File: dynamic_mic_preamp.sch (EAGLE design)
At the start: 13 parts

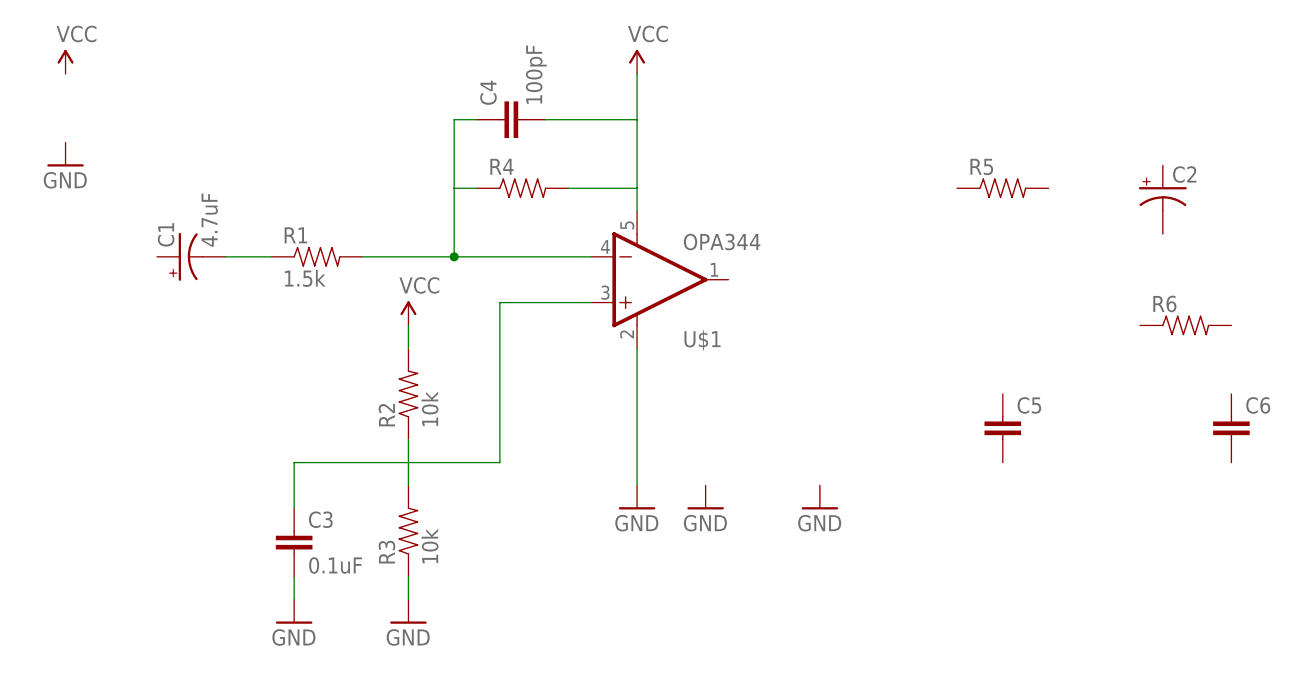
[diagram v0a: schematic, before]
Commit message: roughing out pre-amp schematic
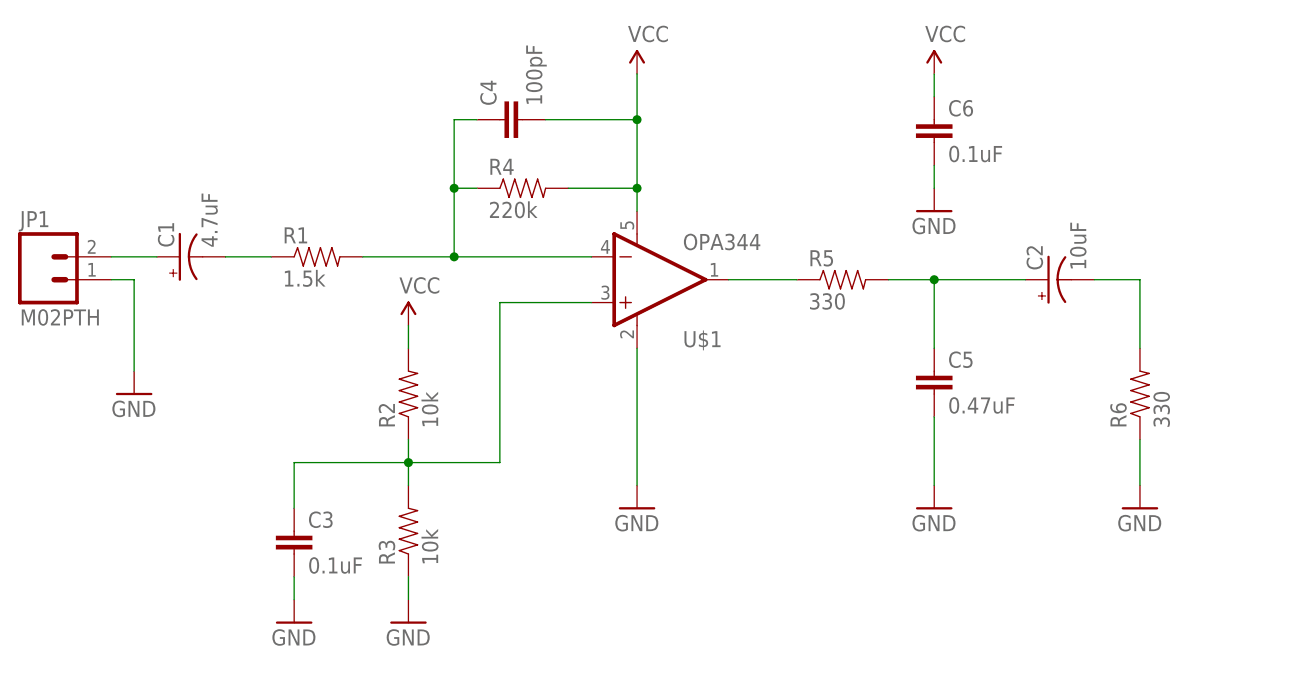
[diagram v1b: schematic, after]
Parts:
- added JP1: M02PTH, SparkFun-Connectors:M02PTH
- C2: value (none) -> 10uF
- C5: value (none) -> 0.47uF
- C6: value (none) -> 0.1uF
- R4: value (none) -> 220k
- R5, R6: value (none) -> 330
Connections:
- new net N$4: R5.1, U$1.OUT
- new net N$5: C2.+, C5.1, R5.2
- new net N$6: C2.-, R6.2
- new net N$7: C1.+, JP1.2
- net GND: now also C5.2, C6.2, JP1.1, R6.1
- net VCC: now also C6.1
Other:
- moved on the sheet: C2, C5, C6, R5, R6
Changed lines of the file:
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@@
 <parts>
 <part name="C1" library="SparkFun-Passives" deviceset="CAP_POL" device="PTH1" value="4.7uF"/>
-<part name="C2" library="SparkFun-Passives" deviceset="CAP_POL" device="PTH1"/>
+<part name="C2" library="SparkFun-Passives" deviceset="CAP_POL" device="PTH1" value="10uF"/>
 <part name="C3" library="SparkFun-Passives" deviceset="CAP" device="PTH" value="0.1uF"/>
 <part name="C4" library="SparkFun-Passives" deviceset="CAP" device="PTH" value="100pF"/>
-<part name="C5" library="SparkFun-Passives" deviceset="CAP" device="PTH"/>
-<part name="C6" library="SparkFun-Passives" deviceset="CAP" device="PTH"/>
+<part name="C5" library="SparkFun-Passives" deviceset="CAP" device="PTH" value="0.47uF"/>
 <part name="U$1" library="SparkFun-AnalogIC" deviceset="OPA344" device=""/>
 <part name="R1" library="SparkFun-Passives" deviceset="RESISTOR" device="PTH-1/4W" value="1.5k"/>
 <part name="R2" library="SparkFun-Passives" deviceset="RESISTOR" device="PTH-1/4W" value="10k"/>
 <part name="R3" library="SparkFun-Passives" deviceset="RESISTOR" device="PTH-1/4W" value="10k"/>
-<part name="R4" library="SparkFun-Passives" deviceset="RESISTOR" device="PTH-1/4W"/>
-<part name="R5" library="SparkFun-Passives" deviceset="RESISTOR" device="PTH-1/4W"/>
-<part name="R6" library="SparkFun-Passives" deviceset="RESISTOR" device="PTH-1/4W"/>
+<part name="R4" library="SparkFun-Passives" deviceset="RESISTOR" device="PTH-1/4W" value="220k"/>
+<part name="R5" library="SparkFun-Passives" deviceset="RESISTOR" device="PTH-1/4W" value="330"/>
+<part name="R6" library="SparkFun-Passives" deviceset="RESISTOR" device="PTH-1/4W" value="330"/>
 <part name="SUPPLY1" library="SparkFun-Aesthetics" deviceset="VCC" device=""/>
 <part name="SUPPLY2" library="SparkFun-Aesthetics" deviceset="VCC" device=""/>
@@
 <part name="GND5" library="SparkFun-Aesthetics" deviceset="GND" device=""/>
 <part name="GND6" library="SparkFun-Aesthetics" deviceset="GND" device=""/>
+<part name="C6" library="SparkFun-Passives" deviceset="CAP" device="PTH" value="0.1uF"/>
+<part name="JP1" library="SparkFun-Connectors" deviceset="M02" device="PTH"/>
+<part name="GND7" library="SparkFun-Aesthetics" deviceset="GND" device=""/>
 </parts>
 <sheets>
@@
 <instances>
 <instance part="C1" gate="G$1" x="7.62" y="73.66" rot="R90"/>
-<instance part="C2" gate="G$1" x="116.84" y="81.28"/>
+<instance part="C2" gate="G$1" x="104.14" y="71.12" rot="R90"/>
 <instance part="C3" gate="G$1" x="20.32" y="40.64"/>
 <instance part="C4" gate="G$1" x="45.72" y="88.9" rot="R90"/>
-<instance part="C5" gate="G$1" x="99.06" y="53.34"/>
-<instance part="C6" gate="G$1" x="124.46" y="53.34"/>
+<instance part="C5" gate="G$1" x="91.44" y="58.42"/>
 <instance part="U$1" gate="G$1" x="58.42" y="71.12"/>
 <instance part="R1" gate="G$1" x="22.86" y="73.66"/>
@@
 <instance part="R3" gate="G$1" x="33.02" y="43.18" rot="R90"/>
 <instance part="R4" gate="G$1" x="45.72" y="81.28"/>
-<instance part="R5" gate="G$1" x="99.06" y="81.28"/>
-<instance part="R6" gate="G$1" x="119.38" y="66.04"/>
+<instance part="R5" gate="G$1" x="81.28" y="71.12"/>
+<instance part="R6" gate="G$1" x="114.3" y="58.42" rot="R90"/>
 <instance part="SUPPLY1" gate="G$1" x="33.02" y="66.04"/>
 <instance part="SUPPLY2" gate="G$1" x="58.42" y="93.98"/>
-<instance part="SUPPLY3" gate="G$1" x="-5.08" y="93.98"/>
-<instance part="GND1" gate="1" x="-5.08" y="83.82"/>
+<instance part="SUPPLY3" gate="G$1" x="91.44" y="93.98"/>
+<instance part="GND1" gate="1" x="91.44" y="78.74"/>
 <instance part="GND2" gate="1" x="33.02" y="33.02"/>
 <instance part="GND3" gate="1" x="20.32" y="33.02"/>
 <instance part="GND4" gate="1" x="58.42" y="45.72"/>
-<instance part="GND5" gate="1" x="66.04" y="45.72"/>
-<instance part="GND6" gate="1" x="78.74" y="45.72"/>
+<instance part="GND5" gate="1" x="91.44" y="45.72"/>
+<instance part="GND6" gate="1" x="114.3" y="45.72"/>
+<instance part="C6" gate="G$1" x="91.44" y="86.36"/>
+<instance part="JP1" gate="G$1" x="-7.62" y="71.12"/>
+<instance part="GND7" gate="1" x="2.54" y="58.42"/>
 </instances>
 <busses>
@@
 <pinref part="U$1" gate="G$1" pin="-IN"/>
 <wire x1="27.94" y1="73.66" x2="38.1" y2="73.66" width="0.1524" layer="91"/>
+<wire x1="38.1" y1="73.66" x2="53.34" y2="73.66" width="0.1524" layer="91"/>
+<junction x="38.1" y="73.66"/>
+<wire x1="38.1" y1="73.66" x2="38.1" y2="81.28" width="0.1524" layer="91"/>
+<pinref part="C4" gate="G$1" pin="1"/>
+<wire x1="38.1" y1="81.28" x2="38.1" y2="88.9" width="0.1524" layer="91"/>
+<wire x1="38.1" y1="88.9" x2="40.64" y2="88.9" width="0.1524" layer="91"/>
 <pinref part="R4" gate="G$1" pin="1"/>
-<wire x1="38.1" y1="73.66" x2="53.34" y2="73.66" width="0.1524" layer="91"/>
 <wire x1="40.64" y1="81.28" x2="38.1" y2="81.28" width="0.1524" layer="91"/>
-<wire x1="38.1" y1="81.28" x2="38.1" y2="73.66" width="0.1524" layer="91"/>
-<junction x="38.1" y="73.66"/>
-<wire x1="38.1" y1="81.28" x2="38.1" y2="88.9" width="0.1524" layer="91"/>
-<pinref part="C4" gate="G$1" pin="1"/>
-<wire x1="38.1" y1="88.9" x2="40.64" y2="88.9" width="0.1524" layer="91"/>
+<junction x="38.1" y="81.28"/>
 </segment>
 </net>
@@
 <pinref part="C4" gate="G$1" pin="2"/>
 <wire x1="48.26" y1="88.9" x2="58.42" y2="88.9" width="0.1524" layer="91"/>
+<junction x="58.42" y="81.28"/>
+<junction x="58.42" y="88.9"/>
+</segment>
+<segment>
+<pinref part="SUPPLY3" gate="G$1" pin="VCC"/>
+<pinref part="C6" gate="G$1" pin="1"/>
+<wire x1="91.44" y1="93.98" x2="91.44" y2="91.44" width="0.1524" layer="91"/>
 </segment>
 </net>
@@
 <pinref part="GND4" gate="1" pin="GND"/>
 <wire x1="58.42" y1="63.5" x2="58.42" y2="48.26" width="0.1524" layer="91"/>
+</segment>
+<segment>
+<pinref part="C5" gate="G$1" pin="2"/>
+<pinref part="GND5" gate="1" pin="GND"/>
+<wire x1="91.44" y1="55.88" x2="91.44" y2="48.26" width="0.1524" layer="91"/>
+</segment>
+<segment>
+<pinref part="GND6" gate="1" pin="GND"/>
+<pinref part="R6" gate="G$1" pin="1"/>
+<wire x1="114.3" y1="48.26" x2="114.3" y2="53.34" width="0.1524" layer="91"/>
+</segment>
+<segment>
+<pinref part="C6" gate="G$1" pin="2"/>
+<pinref part="GND1" gate="1" pin="GND"/>
+<wire x1="91.44" y1="83.82" x2="91.44" y2="81.28" width="0.1524" layer="91"/>
+</segment>
+<segment>
+<pinref part="JP1" gate="G$1" pin="1"/>
+<pinref part="GND7" gate="1" pin="GND"/>
+<wire x1="0" y1="71.12" x2="2.54" y2="71.12" width="0.1524" layer="91"/>
+<wire x1="2.54" y1="71.12" x2="2.54" y2="60.96" width="0.1524" layer="91"/>
 </segment>
 </net>
@@
 <wire x1="20.32" y1="45.72" x2="20.32" y2="50.8" width="0.1524" layer="91"/>
 <wire x1="20.32" y1="50.8" x2="33.02" y2="50.8" width="0.1524" layer="91"/>
+<junction x="33.02" y="50.8"/>
+</segment>
+</net>
+<net name="N$4" class="0">
+<segment>
+<pinref part="U$1" gate="G$1" pin="OUT"/>
+<pinref part="R5" gate="G$1" pin="1"/>
+<wire x1="68.58" y1="71.12" x2="76.2" y2="71.12" width="0.1524" layer="91"/>
+</segment>
+</net>
+<net name="N$5" class="0">
+<segment>
+<pinref part="R5" gate="G$1" pin="2"/>
+<wire x1="86.36" y1="71.12" x2="91.44" y2="71.12" width="0.1524" layer="91"/>
+<pinref part="C5" gate="G$1" pin="1"/>
+<wire x1="91.44" y1="71.12" x2="91.44" y2="63.5" width="0.1524" layer="91"/>
+<pinref part="C2" gate="G$1" pin="+"/>
+<wire x1="91.44" y1="71.12" x2="101.6" y2="71.12" width="0.1524" layer="91"/>
+<junction x="91.44" y="71.12"/>
+</segment>
+</net>
+<net name="N$6" class="0">
+<segment>
+<pinref part="C2" gate="G$1" pin="-"/>
+<pinref part="R6" gate="G$1" pin="2"/>
+<wire x1="109.22" y1="71.12" x2="114.3" y2="71.12" width="0.1524" layer="91"/>
+<wire x1="114.3" y1="71.12" x2="114.3" y2="63.5" width="0.1524" layer="91"/>
+</segment>
+</net>
+<net name="N$7" class="0">
+<segment>
+<pinref part="JP1" gate="G$1" pin="2"/>
+<pinref part="C1" gate="G$1" pin="+"/>
+<wire x1="0" y1="73.66" x2="5.08" y2="73.66" width="0.1524" layer="91"/>
 </segment>
 </net>
@@
 </sheet>
 </sheets>
+<errors>
+</errors>
 </schematic>
 </drawing>

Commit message: udpated schematic for pre-amp
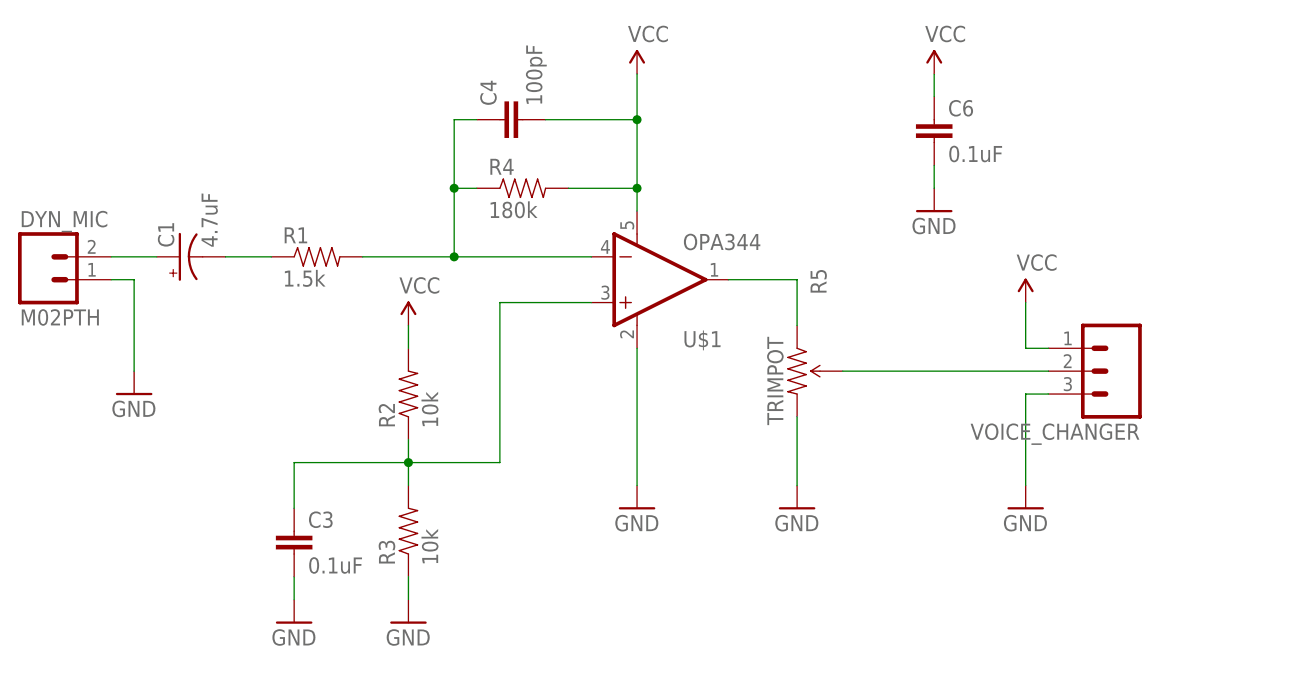
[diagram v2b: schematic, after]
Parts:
- removed C2: 10uF, SparkFun-Passives:CAP_POLPTH1
- removed C5: 0.47uF, SparkFun-Passives:CAPPTH
- removed R6: 330, SparkFun-Passives:RESISTORPTH-1/4W
- added VOICE_CHANGER: (no value), SparkFun-Connectors:M03PTH
- R4: value 220k -> 180k
- R5: value 330 -> TRIMPOT; device SparkFun-Passives:RESISTORPTH-1/4W -> SparkFun-Electromechanical:TRIMPOT
- renumbered JP1 to DYN_MIC
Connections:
- removed net N$6: C2.-, R6.2
- net GND: now also R5.CW, VOICE_CHANGER.3; no longer C5.2, R6.1
- net N$4: now also R5.CCW; no longer R5.1
- net N$5: now also R5.WIPER, VOICE_CHANGER.2; no longer C2.+, C5.1, R5.2
- net VCC: now also VOICE_CHANGER.1
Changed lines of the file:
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@@
 <parts>
 <part name="C1" library="SparkFun-Passives" deviceset="CAP_POL" device="PTH1" value="4.7uF"/>
-<part name="C2" library="SparkFun-Passives" deviceset="CAP_POL" device="PTH1" value="10uF"/>
 <part name="C3" library="SparkFun-Passives" deviceset="CAP" device="PTH" value="0.1uF"/>
 <part name="C4" library="SparkFun-Passives" deviceset="CAP" device="PTH" value="100pF"/>
-<part name="C5" library="SparkFun-Passives" deviceset="CAP" device="PTH" value="0.47uF"/>
 <part name="U$1" library="SparkFun-AnalogIC" deviceset="OPA344" device=""/>
 <part name="R1" library="SparkFun-Passives" deviceset="RESISTOR" device="PTH-1/4W" value="1.5k"/>
 <part name="R2" library="SparkFun-Passives" deviceset="RESISTOR" device="PTH-1/4W" value="10k"/>
 <part name="R3" library="SparkFun-Passives" deviceset="RESISTOR" device="PTH-1/4W" value="10k"/>
-<part name="R4" library="SparkFun-Passives" deviceset="RESISTOR" device="PTH-1/4W" value="220k"/>
-<part name="R5" library="SparkFun-Passives" deviceset="RESISTOR" device="PTH-1/4W" value="330"/>
-<part name="R6" library="SparkFun-Passives" deviceset="RESISTOR" device="PTH-1/4W" value="330"/>
+<part name="R4" library="SparkFun-Passives" deviceset="RESISTOR" device="PTH-1/4W" value="180k"/>
 <part name="SUPPLY1" library="SparkFun-Aesthetics" deviceset="VCC" device=""/>
 <part name="SUPPLY2" library="SparkFun-Aesthetics" deviceset="VCC" device=""/>
@@
 <part name="GND4" library="SparkFun-Aesthetics" deviceset="GND" device=""/>
 <part name="GND5" library="SparkFun-Aesthetics" deviceset="GND" device=""/>
+<part name="C6" library="SparkFun-Passives" deviceset="CAP" device="PTH" value="0.1uF"/>
+<part name="DYN_MIC" library="SparkFun-Connectors" deviceset="M02" device="PTH"/>
+<part name="GND7" library="SparkFun-Aesthetics" deviceset="GND" device=""/>
+<part name="R5" library="SparkFun-Electromechanical" deviceset="TRIMPOT" device=""/>
+<part name="VOICE_CHANGER" library="SparkFun-Connectors" deviceset="M03" device="PTH"/>
+<part name="SUPPLY4" library="SparkFun-Aesthetics" deviceset="VCC" device=""/>
 <part name="GND6" library="SparkFun-Aesthetics" deviceset="GND" device=""/>
-<part name="C6" library="SparkFun-Passives" deviceset="CAP" device="PTH" value="0.1uF"/>
-<part name="JP1" library="SparkFun-Connectors" deviceset="M02" device="PTH"/>
-<part name="GND7" library="SparkFun-Aesthetics" deviceset="GND" device=""/>
 </parts>
 <sheets>
@@
 <instances>
 <instance part="C1" gate="G$1" x="7.62" y="73.66" rot="R90"/>
-<instance part="C2" gate="G$1" x="104.14" y="71.12" rot="R90"/>
 <instance part="C3" gate="G$1" x="20.32" y="40.64"/>
 <instance part="C4" gate="G$1" x="45.72" y="88.9" rot="R90"/>
-<instance part="C5" gate="G$1" x="91.44" y="58.42"/>
 <instance part="U$1" gate="G$1" x="58.42" y="71.12"/>
 <instance part="R1" gate="G$1" x="22.86" y="73.66"/>
@@
 <instance part="R3" gate="G$1" x="33.02" y="43.18" rot="R90"/>
 <instance part="R4" gate="G$1" x="45.72" y="81.28"/>
-<instance part="R5" gate="G$1" x="81.28" y="71.12"/>
-<instance part="R6" gate="G$1" x="114.3" y="58.42" rot="R90"/>
 <instance part="SUPPLY1" gate="G$1" x="33.02" y="66.04"/>
 <instance part="SUPPLY2" gate="G$1" x="58.42" y="93.98"/>
@@
 <instance part="GND3" gate="1" x="20.32" y="33.02"/>
 <instance part="GND4" gate="1" x="58.42" y="45.72"/>
-<instance part="GND5" gate="1" x="91.44" y="45.72"/>
-<instance part="GND6" gate="1" x="114.3" y="45.72"/>
+<instance part="GND5" gate="1" x="76.2" y="45.72"/>
 <instance part="C6" gate="G$1" x="91.44" y="86.36"/>
-<instance part="JP1" gate="G$1" x="-7.62" y="71.12"/>
+<instance part="DYN_MIC" gate="G$1" x="-7.62" y="71.12"/>
 <instance part="GND7" gate="1" x="2.54" y="58.42"/>
+<instance part="R5" gate="R?" x="76.2" y="60.96" rot="R270"/>
+<instance part="VOICE_CHANGER" gate="G$1" x="111.76" y="60.96" rot="R180"/>
+<instance part="SUPPLY4" gate="G$1" x="101.6" y="68.58"/>
+<instance part="GND6" gate="1" x="101.6" y="45.72"/>
 </instances>
 <busses>
@@
 <wire x1="91.44" y1="93.98" x2="91.44" y2="91.44" width="0.1524" layer="91"/>
 </segment>
+<segment>
+<pinref part="SUPPLY4" gate="G$1" pin="VCC"/>
+<wire x1="101.6" y1="68.58" x2="101.6" y2="63.5" width="0.1524" layer="91"/>
+<pinref part="VOICE_CHANGER" gate="G$1" pin="1"/>
+<wire x1="101.6" y1="63.5" x2="104.14" y2="63.5" width="0.1524" layer="91"/>
+</segment>
 </net>
 <net name="GND" class="0">
@@
 </segment>
 <segment>
-<pinref part="C5" gate="G$1" pin="2"/>
-<pinref part="GND5" gate="1" pin="GND"/>
-<wire x1="91.44" y1="55.88" x2="91.44" y2="48.26" width="0.1524" layer="91"/>
-</segment>
-<segment>
-<pinref part="GND6" gate="1" pin="GND"/>
-<pinref part="R6" gate="G$1" pin="1"/>
-<wire x1="114.3" y1="48.26" x2="114.3" y2="53.34" width="0.1524" layer="91"/>
-</segment>
-<segment>
 <pinref part="C6" gate="G$1" pin="2"/>
 <pinref part="GND1" gate="1" pin="GND"/>
@@
 </segment>
 <segment>
-<pinref part="JP1" gate="G$1" pin="1"/>
+<pinref part="DYN_MIC" gate="G$1" pin="1"/>
 <pinref part="GND7" gate="1" pin="GND"/>
 <wire x1="0" y1="71.12" x2="2.54" y2="71.12" width="0.1524" layer="91"/>
 <wire x1="2.54" y1="71.12" x2="2.54" y2="60.96" width="0.1524" layer="91"/>
+</segment>
+<segment>
+<pinref part="R5" gate="R?" pin="CW"/>
+<pinref part="GND5" gate="1" pin="GND"/>
+<wire x1="76.2" y1="55.88" x2="76.2" y2="48.26" width="0.1524" layer="91"/>
+</segment>
+<segment>
+<pinref part="GND6" gate="1" pin="GND"/>
+<wire x1="101.6" y1="48.26" x2="101.6" y2="58.42" width="0.1524" layer="91"/>
+<pinref part="VOICE_CHANGER" gate="G$1" pin="3"/>
+<wire x1="101.6" y1="58.42" x2="104.14" y2="58.42" width="0.1524" layer="91"/>
 </segment>
 </net>
@@
 </segment>
 </net>
+<net name="N$7" class="0">
+<segment>
+<pinref part="DYN_MIC" gate="G$1" pin="2"/>
+<pinref part="C1" gate="G$1" pin="+"/>
+<wire x1="0" y1="73.66" x2="5.08" y2="73.66" width="0.1524" layer="91"/>
+</segment>
+</net>
 <net name="N$4" class="0">
 <segment>
 <pinref part="U$1" gate="G$1" pin="OUT"/>
-<pinref part="R5" gate="G$1" pin="1"/>
+<pinref part="R5" gate="R?" pin="CCW"/>
 <wire x1="68.58" y1="71.12" x2="76.2" y2="71.12" width="0.1524" layer="91"/>
+<wire x1="76.2" y1="71.12" x2="76.2" y2="66.04" width="0.1524" layer="91"/>
 </segment>
 </net>
 <net name="N$5" class="0">
 <segment>
-<pinref part="R5" gate="G$1" pin="2"/>
-<wire x1="86.36" y1="71.12" x2="91.44" y2="71.12" width="0.1524" layer="91"/>
-<pinref part="C5" gate="G$1" pin="1"/>
-<wire x1="91.44" y1="71.12" x2="91.44" y2="63.5" width="0.1524" layer="91"/>
-<pinref part="C2" gate="G$1" pin="+"/>
-<wire x1="91.44" y1="71.12" x2="101.6" y2="71.12" width="0.1524" layer="91"/>
-<junction x="91.44" y="71.12"/>
+<pinref part="R5" gate="R?" pin="WIPER"/>
+<pinref part="VOICE_CHANGER" gate="G$1" pin="2"/>
+<wire x1="81.28" y1="60.96" x2="104.14" y2="60.96" width="0.1524" layer="91"/>
 </segment>
 </net>
-<net name="N$6" class="0">
-<segment>
-<pinref part="C2" gate="G$1" pin="-"/>
-<pinref part="R6" gate="G$1" pin="2"/>
-<wire x1="109.22" y1="71.12" x2="114.3" y2="71.12" width="0.1524" layer="91"/>
-<wire x1="114.3" y1="71.12" x2="114.3" y2="63.5" width="0.1524" layer="91"/>
-</segment>
-</net>
-<net name="N$7" class="0">
-<segment>
-<pinref part="JP1" gate="G$1" pin="2"/>
-<pinref part="C1" gate="G$1" pin="+"/>
-<wire x1="0" y1="73.66" x2="5.08" y2="73.66" width="0.1524" layer="91"/>
-</segment>
-</net>
